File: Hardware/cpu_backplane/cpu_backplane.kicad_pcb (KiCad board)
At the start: 2 copper layers, 149.9 x 99.9 mm, 86 parts, among them J1 USB_B_Micro, J2 Conn_02x02_Odd_Even, J3 Conn_01x06, J4 Conn_01x14, SW1 SW_SPST, U1 74AC161, U2 MAX811SEUS-T, U3 MAX811SEUS-T, U4 PAL24, U5 GAL16V8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

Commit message: update opl2 board status
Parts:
- C6: value 47n -> 1u
- R10, R11, R12, R13, R9: value 470R -> 330R
- R16: value 4.7k -> 2.2K
- SLOT0, SLOT1, SLOT2, SLOT3, SLOT4, SLOT5: value Conn_01x40 -> Conn_02x25

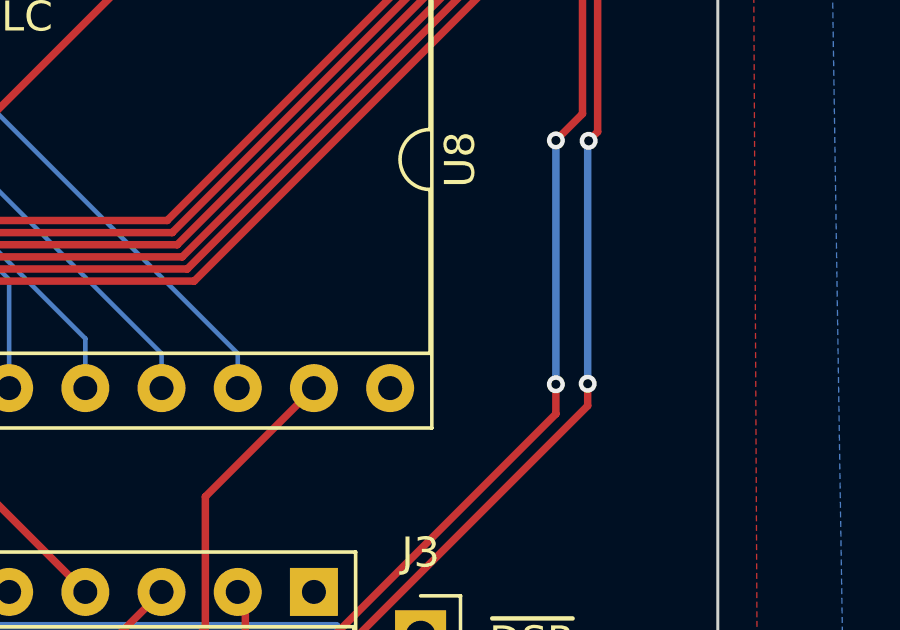
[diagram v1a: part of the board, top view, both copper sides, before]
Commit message: add one capacitor for ROM
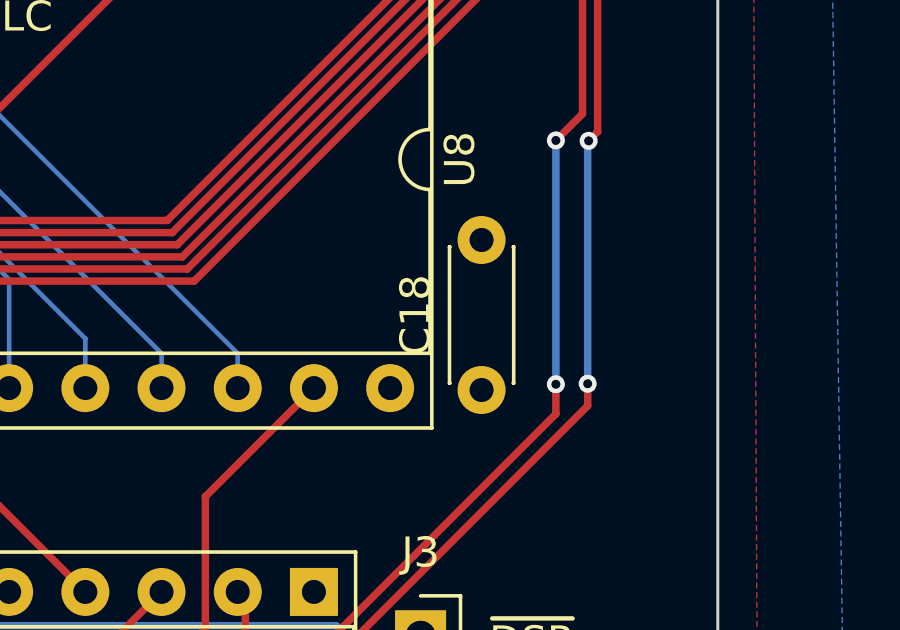
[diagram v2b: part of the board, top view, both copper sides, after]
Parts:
- added C18: 10n, Capacitor_THT:C_Disc_D4.3mm_W1.9mm_P5.00mm, F.Cu at (142.0, 75.2)

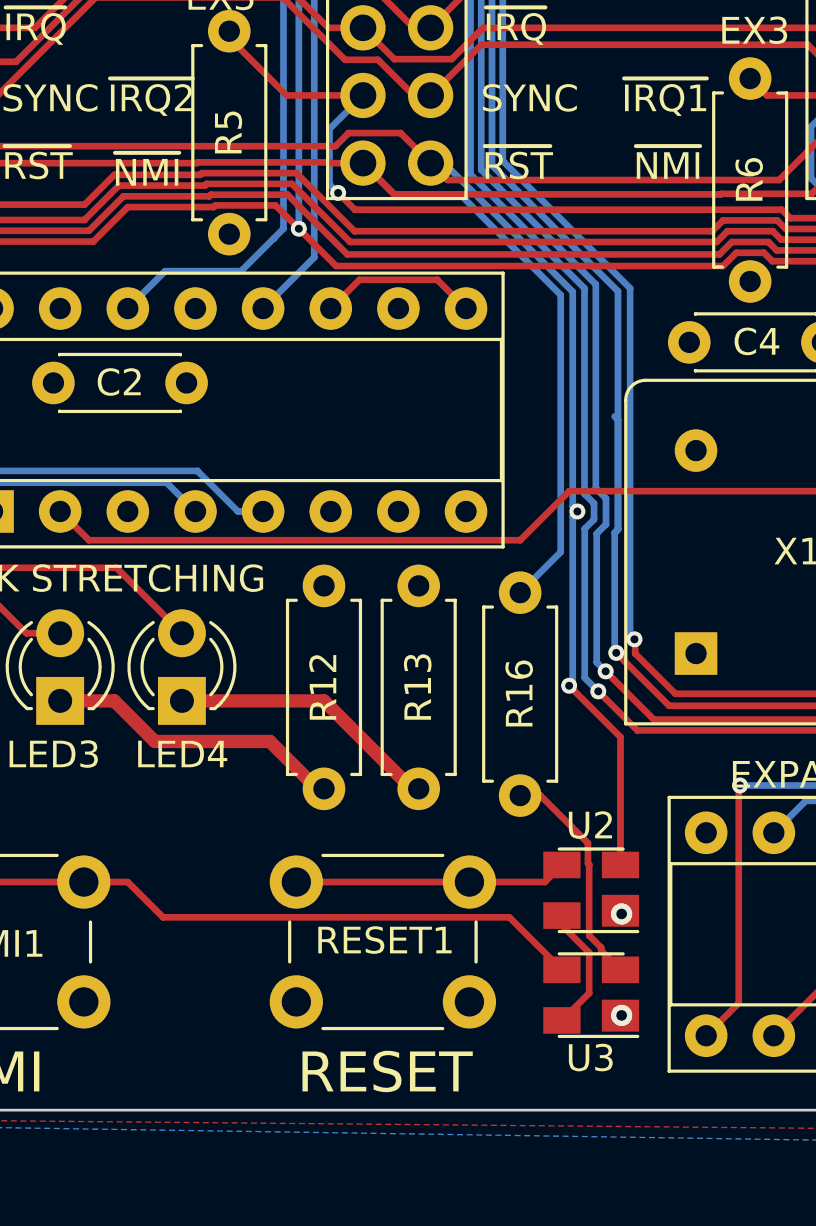
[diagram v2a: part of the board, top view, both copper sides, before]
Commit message: update reset and NMI circuits to through hole DS1813
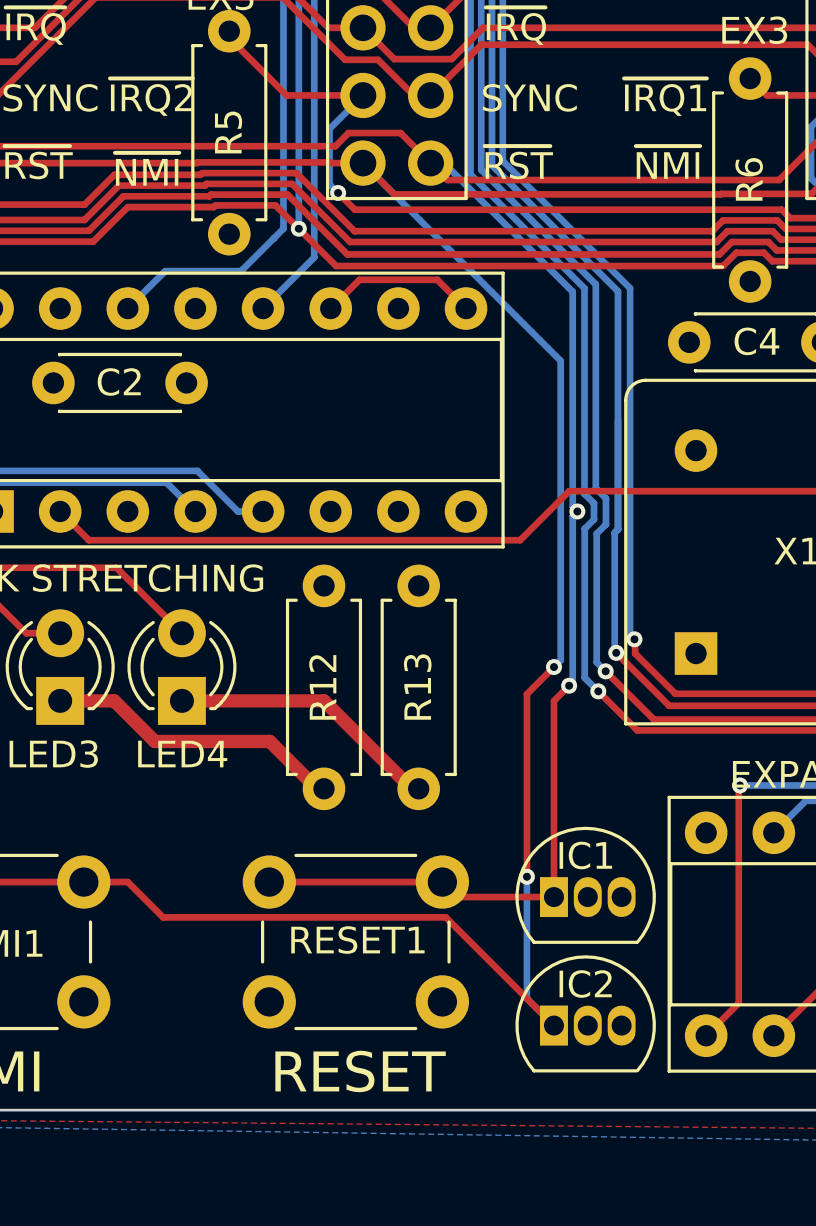
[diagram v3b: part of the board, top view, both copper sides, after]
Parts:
- removed R16: 2.2K, Resistor_THT:R_Axial_DIN0207_L6.3mm_D2.5mm_P7.62mm_Horizontal
- removed U2, U3: MAX811SEUS-T, Package_TO_SOT_SMD:SOT-143
- added IC1: DS1813-10+, Package_TO_SOT_THT:TO-92L_Inline, F.Cu at (64.0, 91.9)
- added IC2: DS1813-10+, Package_TO_SOT_THT:TO-92L_Inline, F.Cu at (64.0, 96.8)
- moved RESET1 1.02 mm to (59.8, 95.9)
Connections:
- NMI1 pad 2: Net-(NMI1-Pad2) -> ~NMI~
- RESET1 pad 2: Net-(RESET1-Pad2) -> ~RESET~
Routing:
- net ~NMI~: track 174.3 -> 215.8 mm, vias 3 -> 5
- net Net-(NMI1-Pad2): track 25.8 -> 0.00 mm
- net ~RESET~: track 258.7 -> 270.0 mm
- net Net-(RESET1-Pad2): track 10.2 -> 0.00 mm
- net Net-(R16-Pad2): track 9.10 -> 0.00 mm
- net +5V: track 144.1 -> 139.3 mm
- net GND: vias 4 -> 2

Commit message: DS1813
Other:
- board text added: "REV. 1.1"
- board text removed: "REV. 1.0"
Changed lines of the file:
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@@
     (effects (font (size 1 1) (thickness 0.15)) (justify right))
   )
-  (gr_text "REV. 1.0" (at 26.67 79.502) (layer F.SilkS)
+  (gr_text "REV. 1.1" (at 26.67 79.502) (layer F.SilkS)
     (effects (font (size 1.5 1.5) (thickness 0.2) italic) (justify right))
   )

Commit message: try to add kibot
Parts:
- added Q1: 2N3905, Package_TO_SOT_THT:TO-92_Inline, F.Cu at (14.9, 91.8)
- added R16: 4.7k, Resistor_THT:R_Axial_DIN0207_L6.3mm_D2.5mm_P7.62mm_Horizontal, F.Cu at (62.2, 80.3)
- added R7: 10k, Resistor_THT:R_Axial_DIN0207_L6.3mm_D2.5mm_P7.62mm_Horizontal, F.Cu at (11.4, 95.9)
- C6: value 1u -> 47n
- IC1: value DS1813-10+ -> DS1813
- IC2: value DS1813-10+ -> DS1813; footprint Package_TO_SOT_THT:TO-92L_Inline -> Package_TO_SOT_THT:TO-92_Inline
- J1: value USB_B_Micro -> Barrel_Jack; footprint Connector_USB:USB_Micro-B_Molex-105017-0001 -> Connector_BarrelJack:BarrelJack_Horizontal
- R10, R11, R12, R13, R9: value 330R -> 470R
- R27: footprint Resistor_THT:R_Axial_DIN0207_L6.3mm_D2.5mm_P7.62mm_Horizontal -> Resistor_THT:R_Axial_DIN0204_L3.6mm_D1.6mm_P5.08mm_Horizontal
- SLOT0, SLOT1, SLOT2, SLOT3, SLOT4, SLOT5: value Conn_02x25 -> Conn_01x40
- moved REF** 151.9 mm to (145.5, 17.3), turned to 90 degrees
- moved J1 7.60 mm to (10.2, 85.7), turned to 0 degrees
- moved C13 2.26 mm to (17.5, 83.8)
- moved IC2 0.20 mm to (63.9, 96.6)
- moved IC1 0.08 mm to (64.0, 91.9)
- renumbered G*** to G1, G*** to G2
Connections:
- net /~CTS~ renamed /~{CTS}
- net /~DSR~ renamed /~{DSR}
- net /~RTS~ renamed /~{RTS}
- net R~W~ renamed R~{W}
- net ~INH~ renamed ~{INH}
- net ~IRQ0~ renamed ~{IRQ0}
- net ~IRQ1~ renamed ~{IRQ1}
- net ~IRQ2~ renamed ~{IRQ2}
- net ~IRQ3~ renamed ~{IRQ3}
- net ~IRQ4~ renamed ~{IRQ4}
- net ~IRQ5~ renamed ~{IRQ5}
- net ~IRQ~ renamed ~{IRQ}
- net ~RAMW~ renamed ~{RAMW}
- net ~RAM_CS~ renamed ~{RAM_CS}
- net ~RESET~ renamed ~{RESET}
- net ~ROM_CS~ renamed ~{ROM_CS}
- net ~SER_IRQ~ renamed ~{SER_IRQ}
- net ~SER~ renamed ~{SER}
- net ~SIRQ~ renamed ~{SIRQ}
- net ~SLOT0~ renamed ~{SLOT0}
- net ~SLOT1~ renamed ~{SLOT1}
- net ~SLOT2~ renamed ~{SLOT2}
- net ~SLOT3~ renamed ~{SLOT3}
- net ~SLOT4~ renamed ~{SLOT4}
- net ~SLOT5~ renamed ~{SLOT5}
- net ~SLOW~ renamed ~{SLOW}
- net ~SSEL~ renamed ~{SSEL}
- IC2 pad 1: ~NMI~ -> Net-(IC2-Pad1)
- J1 pad 2: Net-(J1-Pad2) -> GND
- J1 pad 3: Net-(J1-Pad3) -> (no net)
- NMI1 pad 2: ~NMI~ -> Net-(IC2-Pad1)
- SLOT0 pad 50: ~NMI~ -> ~{NMI}
- SLOT1 pad 50: ~NMI~ -> ~{NMI}
- SLOT2 pad 50: ~NMI~ -> ~{NMI}
- SLOT3 pad 50: ~NMI~ -> ~{NMI}
- SLOT4 pad 50: ~NMI~ -> ~{NMI}
- SLOT5 pad 50: ~NMI~ -> ~{NMI}
- SW1 pad 1: Net-(J1-Pad1) -> Net-(SW1-Pad1)
- U1 pad 13: Net-(U1-Pad13) -> unconnected-(U1-Pad13)
- U1 pad 15: Net-(U1-Pad15) -> unconnected-(U1-Pad15)
- U4 pad 16: Net-(U4-Pad16) -> unconnected-(U4-Pad16)
- U5 pad 15: Net-(U5-Pad15) -> unconnected-(U5-Pad15)
- U6 pad 1: Net-(U6-Pad1) -> unconnected-(U6-Pad1)
- U6 pad 3: Net-(U6-Pad3) -> unconnected-(U6-Pad3)
- U6 pad 35: Net-(U6-Pad35) -> unconnected-(U6-Pad35)
- U6 pad 39: Net-(U6-Pad39) -> unconnected-(U6-Pad39)
- U6 pad 5: Net-(U6-Pad5) -> unconnected-(U6-Pad5)
- U6 pad 6: ~NMI~ -> ~{NMI}
- U9 pad 11: Net-(U9-Pad11) -> unconnected-(U9-Pad11)
- U9 pad 5: Net-(U9-Pad5) -> unconnected-(U9-Pad5)
- U9 pad 7: Net-(U9-Pad7) -> unconnected-(U9-Pad7)
- X1 pad 1: Net-(X1-Pad1) -> unconnected-(X1-Pad1)
- X3 pad 1: Net-(X3-Pad1) -> unconnected-(X3-Pad1)
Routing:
- net ~NMI~: track 215.8 -> 0.00 mm, vias 5 -> 0
- net ~{NMI}: track 0.00 -> 172.8 mm, vias 0 -> 3
- net Net-(IC2-Pad1): track 0.00 -> 37.6 mm, vias 0 -> 1
- net Net-(J1-Pad1): track 22.6 -> 8.07 mm
- net +5V: track 139.3 -> 148.0 mm
- net GND: track 31.9 -> 24.3 mm
- net Net-(Q1-Pad2): track 0.00 -> 7.16 mm
- net Net-(SW1-Pad1): track 0.00 -> 6.80 mm
- net ~{SSEL}: track 223.2 -> 227.9 mm
- net Net-(R27-Pad2): track 3.24 -> 5.78 mm
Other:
- net class Default removed
- board text added: "REV. 1.2"
- board text added: "R~{W}"
- board text added: "~{DSR}"
- board text added: "~{INH}"
- board text added: "~{IRQ0}"
- board text added: "~{IRQ1}"
- board text added: "~{IRQ2}"
- board text added: "~{IRQ3}"
- board text added: "~{IRQ4}"
- board text added: "~{IRQ}"
- board text added: "~{NMI}"
- board text added: "~{RST}"
- board text added: "~{RTS}"
- board text added: "~{SEL0}"
- board text added: "~{SEL1}"
- board text added: "~{SEL2}"
- board text added: "~{SEL3}"
- board text added: "~{SEL4}"
- board text added: "~{SLOW}"
- board text added: "~{SSEL}"
- board text removed: "REV. 1.1"
- board text removed: "R~W~"
- board text removed: "~DSR~"
- board text removed: "~INH~"
- board text removed: "~IRQ0~"
- board text removed: "~IRQ1~"
- board text removed: "~IRQ2~"
- board text removed: "~IRQ3~"
- board text removed: "~IRQ4~"
- board text removed: "~IRQ~"
- board text removed: "~NMI~"
- board text removed: "~RST~"
- board text removed: "~RTS~"
- board text removed: "~SEL0~"
- board text removed: "~SEL1~"
- board text removed: "~SEL2~"
- board text removed: "~SEL3~"
- board text removed: "~SEL4~"
- board text removed: "~SLOW~"
- board text removed: "~SSEL~"

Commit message: update to kicad 6
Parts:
- removed C18: 10n, Capacitor_THT:C_Disc_D4.3mm_W1.9mm_P5.00mm
- removed G1, G2: LOGO, Logo:logo-sm
- removed Q1: 2N3905, Package_TO_SOT_THT:TO-92_Inline
- removed REF**: OSHW-Logo2_7.3x6mm_SilkScreen, Symbol:OSHW-Logo2_7.3x6mm_SilkScreen
- removed REF**: KiCad-Logo2_5mm_SilkScreen, Symbol:KiCad-Logo2_5mm_SilkScreen
- added D9: 1N5822, Diode_THT:D_DO-201AD_P15.24mm_Horizontal, F.Cu at (15.1, 91.6)
- added U2: L7905, Package_TO_SOT_THT:TO-220-3_Vertical, F.Cu at (15.6, 96.1)
- SW1: value SW_SPST -> SW
- moved R7 134.0 mm to (142.4, 67.6), turned to -90 degrees
- moved C13 11.0 mm to (22.1, 93.8)
- moved R9 7.18 mm to (22.5, 87.5), turned to 0 degrees
- moved SW1 6.38 mm to (30.1, 91.2), turned to -90 degrees
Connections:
- R7 pad 1: Net-(Q1-Pad2) -> ~{SER_IRQ}
- R7 pad 2: GND -> +5V
- SW1 pad 2: +5V -> Net-(SW1-Pad2)
- U5 pad 14: ~{SIRQ} -> unconnected-(U5-Pad14)
- U9 pad 26: ~{SIRQ} -> ~{SER_IRQ}
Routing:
- net ~{SIRQ}: track 66.7 -> 0.00 mm, vias 3 -> 0
- net ~{SER_IRQ}: track 0.00 -> 60.4 mm, vias 0 -> 2
- net +5V: track 148.0 -> 127.2 mm
- net Net-(SW1-Pad2): track 0.00 -> 20.6 mm
- net Net-(D9-Pad1): track 6.80 -> 16.3 mm
- net ~{SLOW}: track 201.5 -> 193.8 mm, vias 3 -> 2
- net Net-(Q1-Pad2): track 7.16 -> 0.00 mm
- net ~{SLOT3}: track 102.7 -> 97.6 mm
- net A12: track 241.3 -> 237.3 mm
- net D0: track 259.3 -> 255.6 mm
- net Net-(D9-Pad2): track 8.07 -> 11.4 mm
- net A13: track 256.5 -> 253.5 mm
- net ~{RESET}: track 270.0 -> 267.0 mm, vias 6 -> 5
- net A1: track 250.1 -> 247.7 mm
- net SYNC: track 152.0 -> 150.1 mm
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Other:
- board text added: "${VERSION}"
- board text removed: "REV. 1.2"

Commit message: update for kicad 6
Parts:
- added G***: LOGO, Logo:logo, F.Cu at (14.0, 71.6)
- added REF**: KiCad-Logo2_5mm_SilkScreen, Symbol:KiCad-Logo2_5mm_SilkScreen, F.Cu at (145.2, 15.2)
- added REF**: OSHW-Logo2_7.3x6mm_SilkScreen, Symbol:OSHW-Logo2_7.3x6mm_SilkScreen, F.Cu at (145.3, 26.2)
